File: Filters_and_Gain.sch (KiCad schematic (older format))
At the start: 22 parts, among them U4 OPA388, U5 OPA388, U6 OPA388

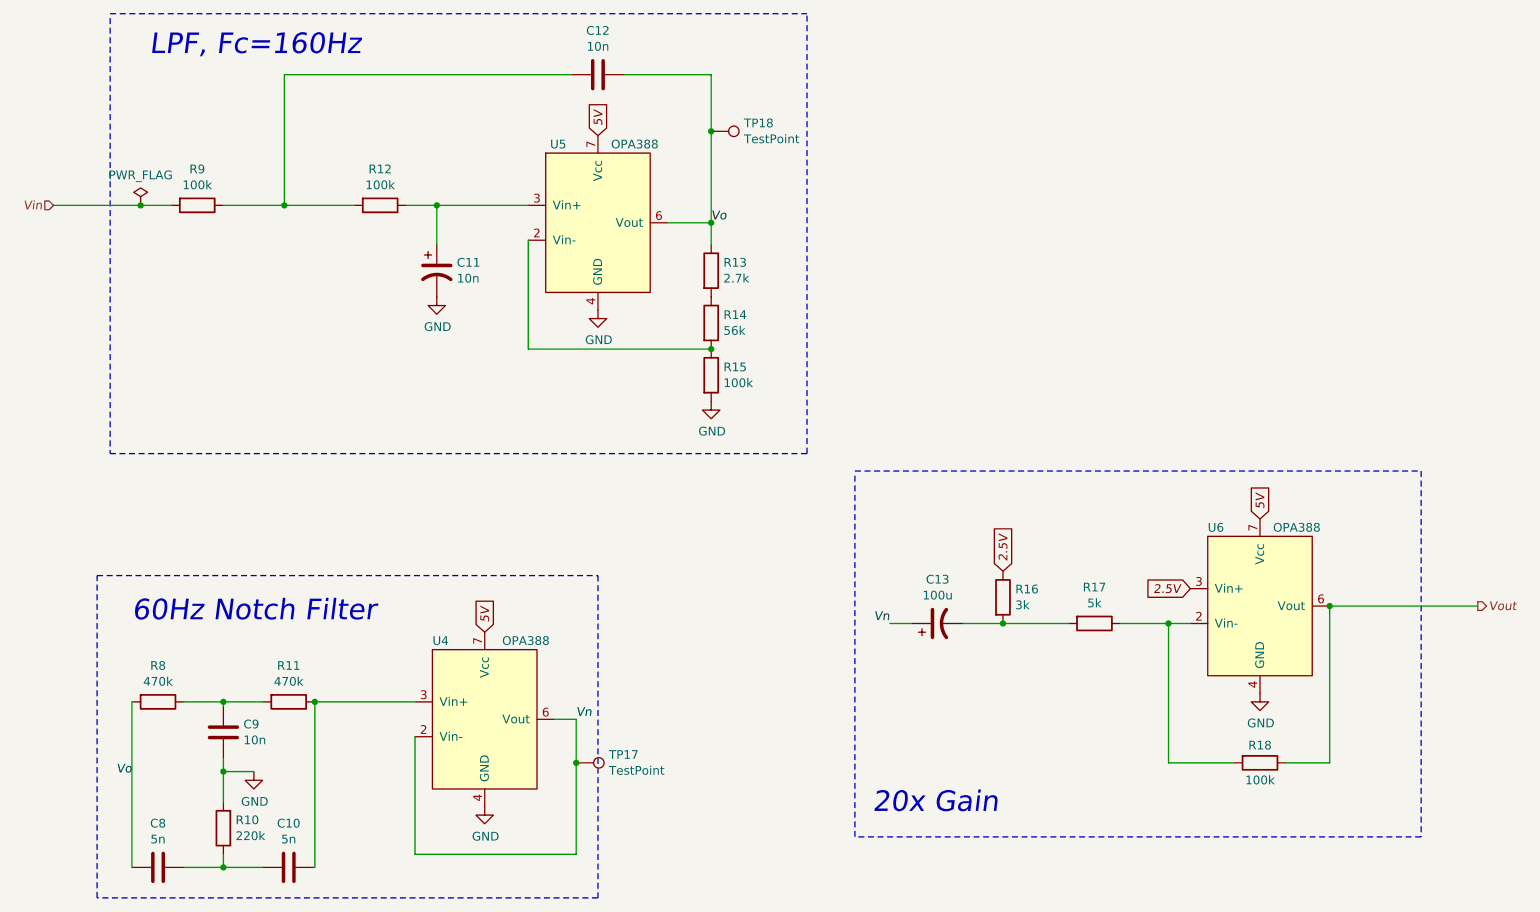
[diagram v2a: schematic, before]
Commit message: Added bypass caps on ICs and fixed the SHDN input.
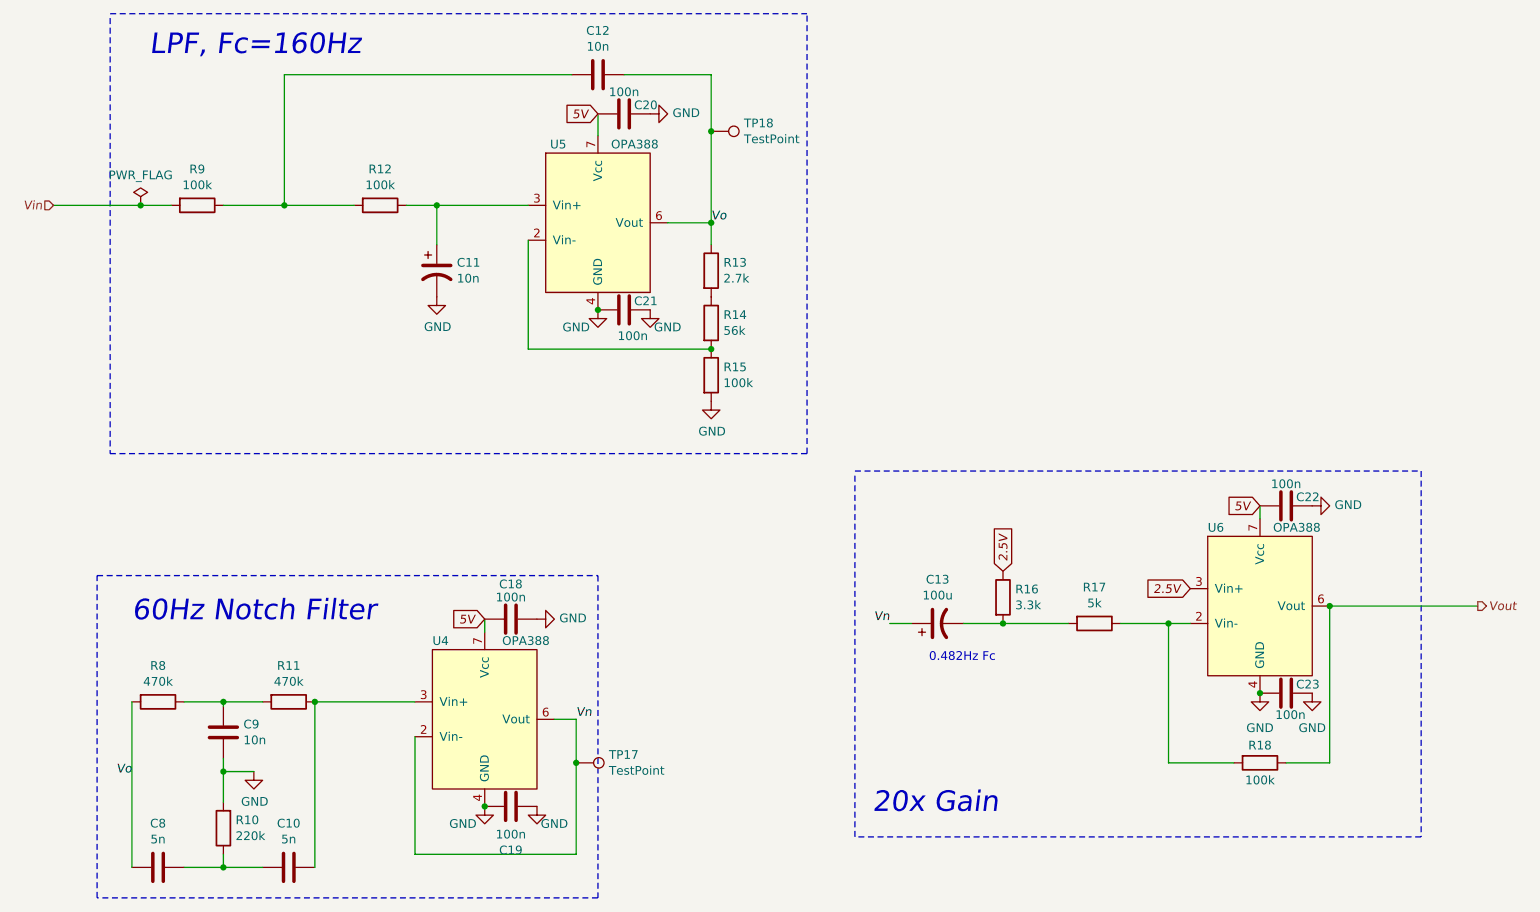
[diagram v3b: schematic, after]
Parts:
- added C18, C19, C20, C21, C22, C23: 100n, Capacitor_SMD:C_0805_2012Metric_Pad1.18x1.45mm_HandSolder, symbol Device:C
- R16: value 3k -> 3.3k
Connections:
- net 5V: now also C18.1, C20.1, C22.1
- net GND: now also C18.2, C19.1, C19.2, C20.2, C21.1, C21.2, C22.2, C23.1, C23.2
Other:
- note added: "0.482Hz Fc"
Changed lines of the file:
@@
 P 4975 2800
 F 0 "#PWR07" H 4975 2550 50  0001 C CNN
-F 1 "GND" H 4980 2627 50  0000 C CNN
+F 1 "GND" H 4850 2700 50  0000 C CNN
 F 2 "" H 4975 2800 50  0001 C CNN
 F 3 "" H 4975 2800 50  0001 C CNN
@@
 	0    -1   -1   0
 $EndComp
-Text GLabel 4975 1800 1    50   Input Italic 0
+Text GLabel 4975 1675 0    50   Input Italic 0
 5V
 Wire Wire Line
@@
 Wire Wire Line
 	4850 5150 4725 5150
-Text GLabel 4325 4650 1    50   Input Italic 0
+Text GLabel 4325 4575 0    50   Input Italic 0
 5V
 $Comp
@@
 P 4325 5650
 F 0 "#PWR06" H 4325 5400 50  0001 C CNN
-F 1 "GND" H 4330 5477 50  0000 C CNN
+F 1 "GND" H 4200 5550 50  0000 C CNN
 F 2 "" H 4325 5650 50  0001 C CNN
 F 3 "" H 4325 5650 50  0001 C CNN
@@
 P 7300 4450
 F 0 "R16" H 7370 4496 50  0000 L CNN
-F 1 "3k" H 7370 4405 50  0000 L CNN
+F 1 "3.3k" H 7370 4405 50  0000 L CNN
 F 2 "Resistor_SMD:R_0805_2012Metric_Pad1.20x1.40mm_HandSolder" V 7230 4450 50  0001 C CNN
 F 3 "~" H 7300 4450 50  0001 C CNN
@@
 Text GLabel 7300 4300 1    50   Input Italic 0
 2.5V
-Text GLabel 8775 4000 1    50   Input Italic 0
+Text GLabel 8775 3925 0    50   Input Italic 0
 5V
 Text Label 6650 4600 2    50   Italic 0
@@
 P 8775 5000
 F 0 "#PWR09" H 8775 4750 50  0001 C CNN
-F 1 "GND" H 8780 4827 50  0000 C CNN
+F 1 "GND" H 8775 4800 50  0000 C CNN
 F 2 "" H 8775 5000 50  0001 C CNN
 F 3 "" H 8775 5000 50  0001 C CNN
@@
 Wire Wire Line
 	4850 5400 4850 5150
+$Comp
+L Device:C C19
+U 1 1 5FCC7188
+P 4475 5650
+F 0 "C19" V 4223 5650 50  0000 C CNN
+F 1 "100n" V 4314 5650 50  0000 C CNN
+F 2 "Capacitor_SMD:C_0805_2012Metric_Pad1.18x1.45mm_HandSolder" H 4513 5500 50  0001 C CNN
+F 3 "~" H 4475 5650 50  0001 C CNN
+	1    4475 5650
+	0    -1   -1   0
+$EndComp
+Connection ~ 4325 5650
+$Comp
+L power:GND #PWR020
+U 1 1 5FCC830B
+P 4625 5650
+F 0 "#PWR020" H 4625 5400 50  0001 C CNN
+F 1 "GND" H 4725 5550 50  0000 C CNN
+F 2 "" H 4625 5650 50  0001 C CNN
+F 3 "" H 4625 5650 50  0001 C CNN
+	1    4625 5650
+	1    0    0    -1
+$EndComp
+$Comp
+L Device:C C18
+U 1 1 5FCC85F8
+P 4475 4575
+F 0 "C18" V 4675 4575 50  0000 C CNN
+F 1 "100n" V 4600 4575 50  0000 C CNN
+F 2 "Capacitor_SMD:C_0805_2012Metric_Pad1.18x1.45mm_HandSolder" H 4513 4425 50  0001 C CNN
+F 3 "~" H 4475 4575 50  0001 C CNN
+	1    4475 4575
+	0    -1   -1   0
+$EndComp
+$Comp
+L power:GND #PWR019
+U 1 1 5FCCCC9D
+P 4625 4575
+F 0 "#PWR019" H 4625 4325 50  0001 C CNN
+F 1 "GND" V 4630 4447 50  0000 R CNN
+F 2 "" H 4625 4575 50  0001 C CNN
+F 3 "" H 4625 4575 50  0001 C CNN
+	1    4625 4575
+	0    -1   -1   0
+$EndComp
+Wire Wire Line
+	4325 4650 4325 4575
+$Comp
+L Device:C C20
+U 1 1 5FCDCCC4
+P 5125 1675
+F 0 "C20" V 5175 1550 50  0000 C CNN
+F 1 "100n" V 5250 1675 50  0000 C CNN
+F 2 "Capacitor_SMD:C_0805_2012Metric_Pad1.18x1.45mm_HandSolder" H 5163 1525 50  0001 C CNN
+F 3 "~" H 5125 1675 50  0001 C CNN
+	1    5125 1675
+	0    -1   -1   0
+$EndComp
+$Comp
+L power:GND #PWR021
+U 1 1 5FCDF168
+P 5275 1675
+F 0 "#PWR021" H 5275 1425 50  0001 C CNN
+F 1 "GND" V 5280 1547 50  0000 R CNN
+F 2 "" H 5275 1675 50  0001 C CNN
+F 3 "" H 5275 1675 50  0001 C CNN
+	1    5275 1675
+	0    -1   -1   0
+$EndComp
+Wire Wire Line
+	4975 1800 4975 1675
+$Comp
+L Device:C C21
+U 1 1 5FCE2857
+P 5125 2800
+F 0 "C21" V 5175 2675 50  0000 C CNN
+F 1 "100n" V 4975 2750 50  0000 C CNN
+F 2 "Capacitor_SMD:C_0805_2012Metric_Pad1.18x1.45mm_HandSolder" H 5163 2650 50  0001 C CNN
+F 3 "~" H 5125 2800 50  0001 C CNN
+	1    5125 2800
+	0    -1   -1   0
+$EndComp
+Connection ~ 4975 2800
+$Comp
+L power:GND #PWR022
+U 1 1 5FCE3A7C
+P 5275 2800
+F 0 "#PWR022" H 5275 2550 50  0001 C CNN
+F 1 "GND" H 5375 2700 50  0000 C CNN
+F 2 "" H 5275 2800 50  0001 C CNN
+F 3 "" H 5275 2800 50  0001 C CNN
+	1    5275 2800
+	1    0    0    -1
+$EndComp
+$Comp
+L Device:C C22
+U 1 1 5FCE4542
+P 8925 3925
+F 0 "C22" V 8975 3800 50  0000 C CNN
+F 1 "100n" V 9050 3925 50  0000 C CNN
+F 2 "Capacitor_SMD:C_0805_2012Metric_Pad1.18x1.45mm_HandSolder" H 8963 3775 50  0001 C CNN
+F 3 "~" H 8925 3925 50  0001 C CNN
+	1    8925 3925
+	0    -1   -1   0
+$EndComp
+Wire Wire Line
+	8775 3925 8775 4000
+$Comp
+L power:GND #PWR023
+U 1 1 5FCE7DE3
+P 9075 3925
+F 0 "#PWR023" H 9075 3675 50  0001 C CNN
+F 1 "GND" V 9080 3797 50  0000 R CNN
+F 2 "" H 9075 3925 50  0001 C CNN
+F 3 "" H 9075 3925 50  0001 C CNN
+	1    9075 3925
+	0    -1   -1   0
+$EndComp
+$Comp
+L Device:C C23
+U 1 1 5FCE8246
+P 8925 5000
+F 0 "C23" V 8975 4875 50  0000 C CNN
+F 1 "100n" V 8800 4975 50  0000 C CNN
+F 2 "Capacitor_SMD:C_0805_2012Metric_Pad1.18x1.45mm_HandSolder" H 8963 4850 50  0001 C CNN
+F 3 "~" H 8925 5000 50  0001 C CNN
+	1    8925 5000
+	0    -1   -1   0
+$EndComp
+Connection ~ 8775 5000
+$Comp
+L power:GND #PWR024
+U 1 1 5FCE9A81
+P 9075 5000
+F 0 "#PWR024" H 9075 4750 50  0001 C CNN
+F 1 "GND" H 9075 4800 50  0000 C CNN
+F 2 "" H 9075 5000 50  0001 C CNN
+F 3 "" H 9075 5000 50  0001 C CNN
+	1    9075 5000
+	1    0    0    -1
+$EndComp
+Text Notes 6875 4825 0    50   ~ 0
+0.482Hz Fc
 $EndSCHEMATC

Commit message: Removed extra caps and removed the tantalum cap as it was too large
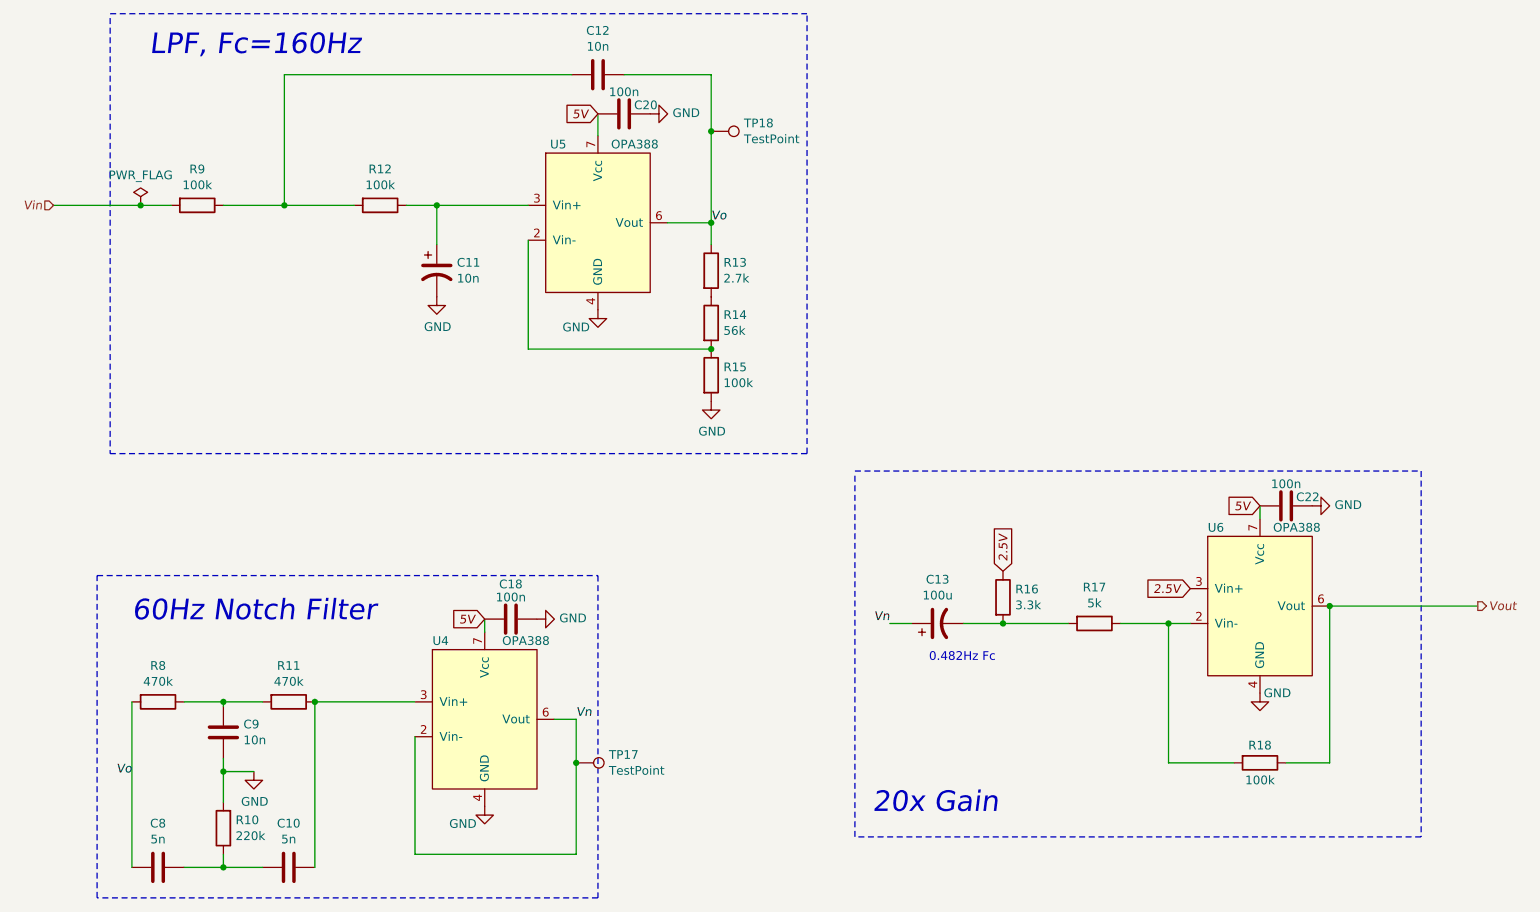
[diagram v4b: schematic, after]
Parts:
- removed C19, C21, C23: 100n, Capacitor_SMD:C_0805_2012Metric_Pad1.18x1.45mm_HandSolder, symbol Device:C
- C13: footprint Capacitor_SMD:CP_Elec_6.3x3 -> Capacitor_SMD:C_1210_3225Metric_Pad1.33x2.70mm_HandSolder
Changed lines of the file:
@@
 F 0 "C13" V 7177 4600 50  0000 C CNN
 F 1 "100u" V 7086 4600 50  0000 C CNN
-F 2 "Capacitor_SMD:CP_Elec_6.3x3" H 6925 4600 50  0001 C CNN
+F 2 "Capacitor_SMD:C_1210_3225Metric_Pad1.33x2.70mm_HandSolder" H 6925 4600 50  0001 C CNN
 F 3 "~" H 6925 4600 50  0001 C CNN
 	1    6925 4600
@@
 P 8775 5000
 F 0 "#PWR09" H 8775 4750 50  0001 C CNN
-F 1 "GND" H 8775 4800 50  0000 C CNN
+F 1 "GND" H 8875 5000 50  0000 C CNN
 F 2 "" H 8775 5000 50  0001 C CNN
 F 3 "" H 8775 5000 50  0001 C CNN
@@
 	4850 5400 4850 5150
 $Comp
-L Device:C C19
-U 1 1 5FCC7188
-P 4475 5650
-F 0 "C19" V 4223 5650 50  0000 C CNN
-F 1 "100n" V 4314 5650 50  0000 C CNN
-F 2 "Capacitor_SMD:C_0805_2012Metric_Pad1.18x1.45mm_HandSolder" H 4513 5500 50  0001 C CNN
-F 3 "~" H 4475 5650 50  0001 C CNN
-	1    4475 5650
-	0    -1   -1   0
-$EndComp
-Connection ~ 4325 5650
-$Comp
-L power:GND #PWR020
-U 1 1 5FCC830B
-P 4625 5650
-F 0 "#PWR020" H 4625 5400 50  0001 C CNN
-F 1 "GND" H 4725 5550 50  0000 C CNN
-F 2 "" H 4625 5650 50  0001 C CNN
-F 3 "" H 4625 5650 50  0001 C CNN
-	1    4625 5650
-	1    0    0    -1
-$EndComp
-$Comp
 L Device:C C18
 U 1 1 5FCC85F8
@@
 	4975 1800 4975 1675
 $Comp
-L Device:C C21
-U 1 1 5FCE2857
-P 5125 2800
-F 0 "C21" V 5175 2675 50  0000 C CNN
-F 1 "100n" V 4975 2750 50  0000 C CNN
-F 2 "Capacitor_SMD:C_0805_2012Metric_Pad1.18x1.45mm_HandSolder" H 5163 2650 50  0001 C CNN
-F 3 "~" H 5125 2800 50  0001 C CNN
-	1    5125 2800
-	0    -1   -1   0
-$EndComp
-Connection ~ 4975 2800
-$Comp
-L power:GND #PWR022
-U 1 1 5FCE3A7C
-P 5275 2800
-F 0 "#PWR022" H 5275 2550 50  0001 C CNN
-F 1 "GND" H 5375 2700 50  0000 C CNN
-F 2 "" H 5275 2800 50  0001 C CNN
-F 3 "" H 5275 2800 50  0001 C CNN
-	1    5275 2800
-	1    0    0    -1
-$EndComp
-$Comp
 L Device:C C22
 U 1 1 5FCE4542
@@
 	0    -1   -1   0
 $EndComp
-$Comp
-L Device:C C23
-U 1 1 5FCE8246
-P 8925 5000
-F 0 "C23" V 8975 4875 50  0000 C CNN
-F 1 "100n" V 8800 4975 50  0000 C CNN
-F 2 "Capacitor_SMD:C_0805_2012Metric_Pad1.18x1.45mm_HandSolder" H 8963 4850 50  0001 C CNN
-F 3 "~" H 8925 5000 50  0001 C CNN
-	1    8925 5000
-	0    -1   -1   0
-$EndComp
-Connection ~ 8775 5000
-$Comp
-L power:GND #PWR024
-U 1 1 5FCE9A81
-P 9075 5000
-F 0 "#PWR024" H 9075 4750 50  0001 C CNN
-F 1 "GND" H 9075 4800 50  0000 C CNN
-F 2 "" H 9075 5000 50  0001 C CNN
-F 3 "" H 9075 5000 50  0001 C CNN
-	1    9075 5000
-	1    0    0    -1
-$EndComp
 Text Notes 6875 4825 0    50   ~ 0

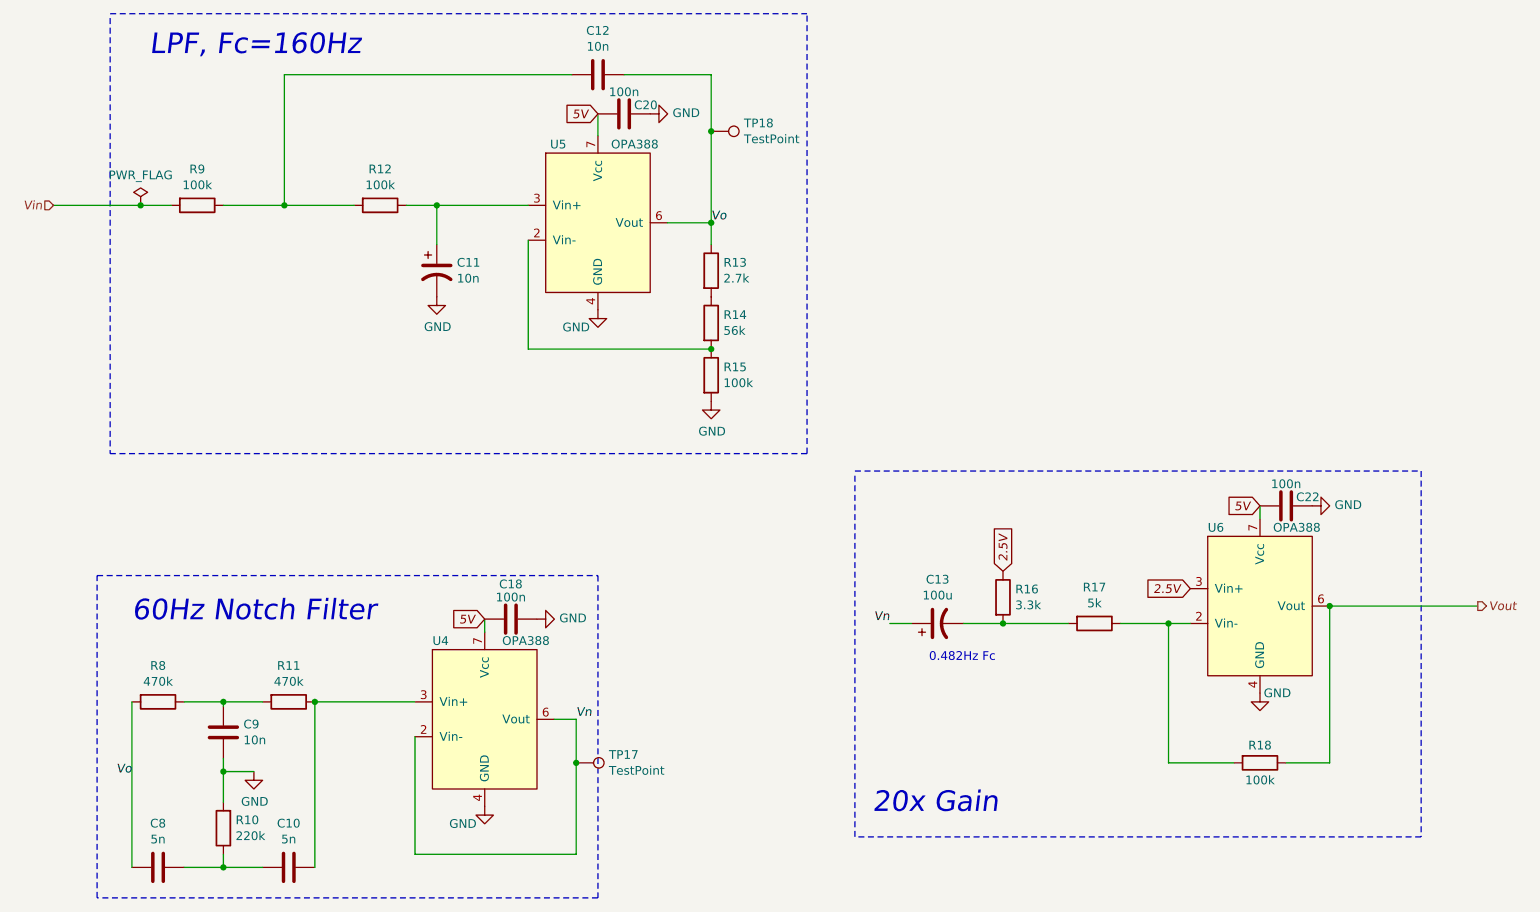
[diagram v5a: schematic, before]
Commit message: #5 - Added 3.3V buck-boost regulator
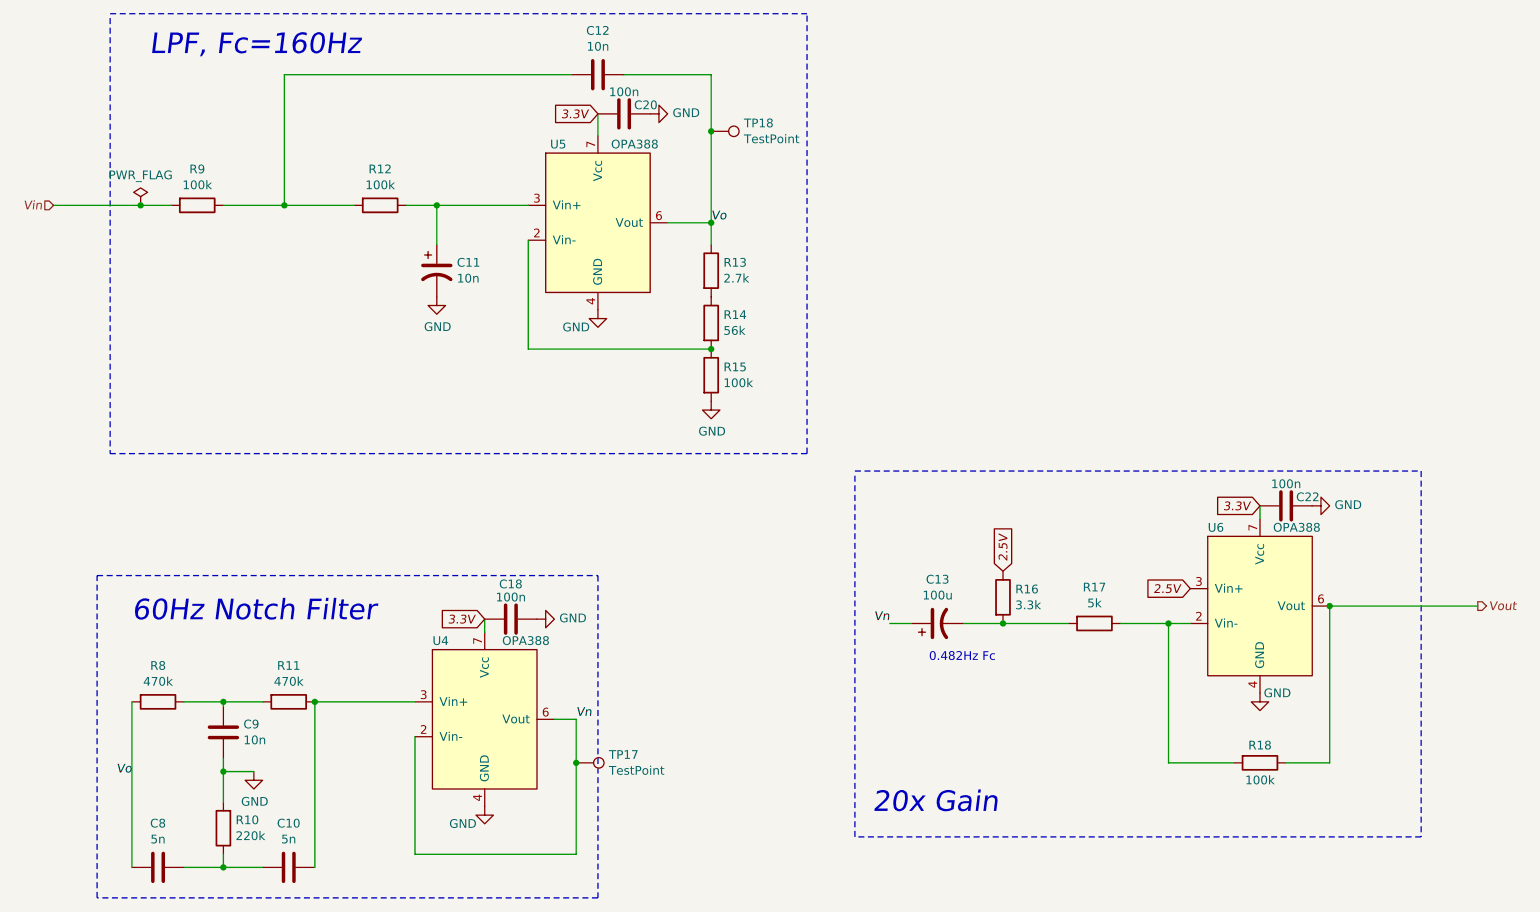
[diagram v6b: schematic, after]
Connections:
- net 5V renamed 3.3V
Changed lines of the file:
@@
 $EndComp
 Text GLabel 4975 1675 0    50   Input Italic 0
-5V
+3.3V
 Wire Wire Line
 	5125 1450 5625 1450
@@
 2.5V
 Text GLabel 8775 3925 0    50   Input Italic 0
-5V
+3.3V
 Text Label 6650 4600 2    50   Italic 0
 Vn
@@
 $EndComp
 Text GLabel 4325 4575 0    50   Input Italic 0
-5V
+3.3V
 Wire Wire Line
 	4850 5150 4725 5150
